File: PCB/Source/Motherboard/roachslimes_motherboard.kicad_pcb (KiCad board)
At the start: 2 copper layers, 34.5 x 49.9 mm, 13 parts, among them J1 Conn_01x04_Pin, J2 Conn_01x02_Pin, J3 Conn_01x03_Pin, SW1 SK12D07VG4, U1 WeMos_D1_mini, U2 TP4056_Board, U3 BMI160_Board, U4 GY-271

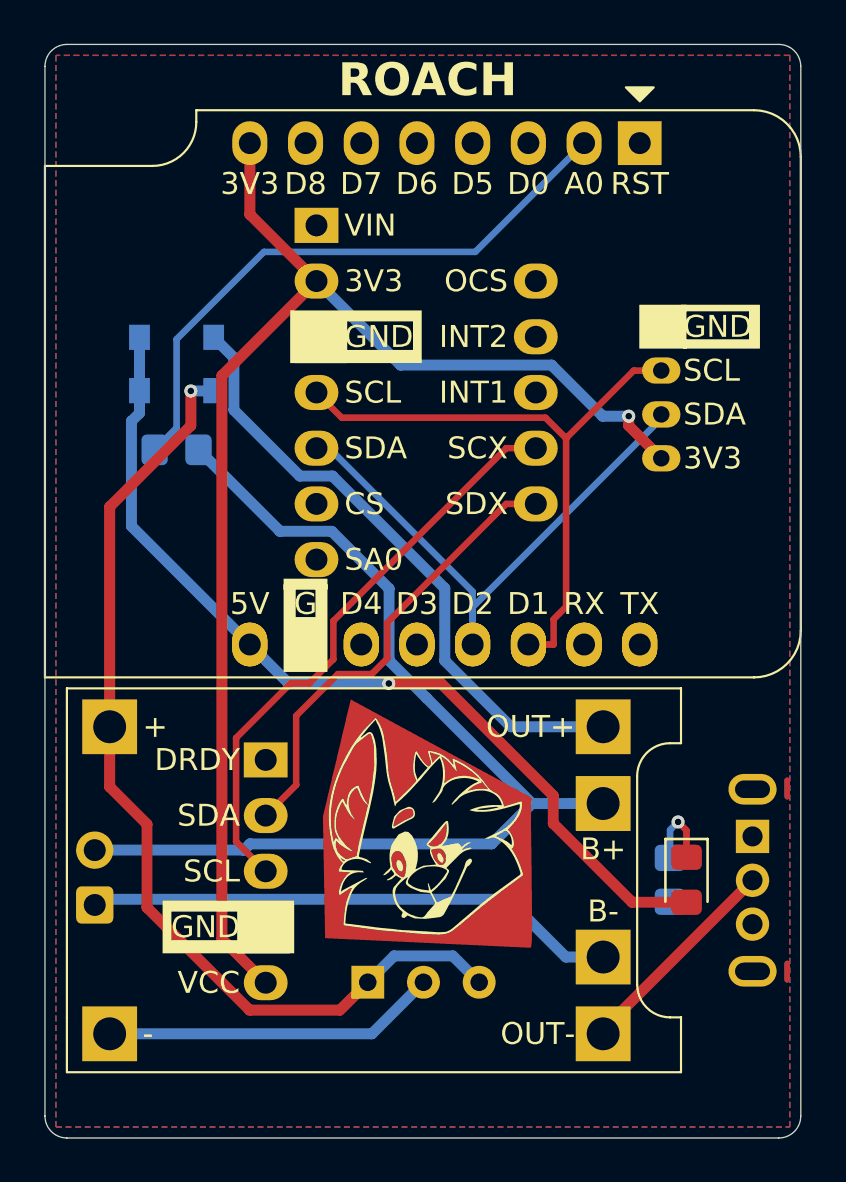
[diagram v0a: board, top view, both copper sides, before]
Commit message: fix minor spelling issues
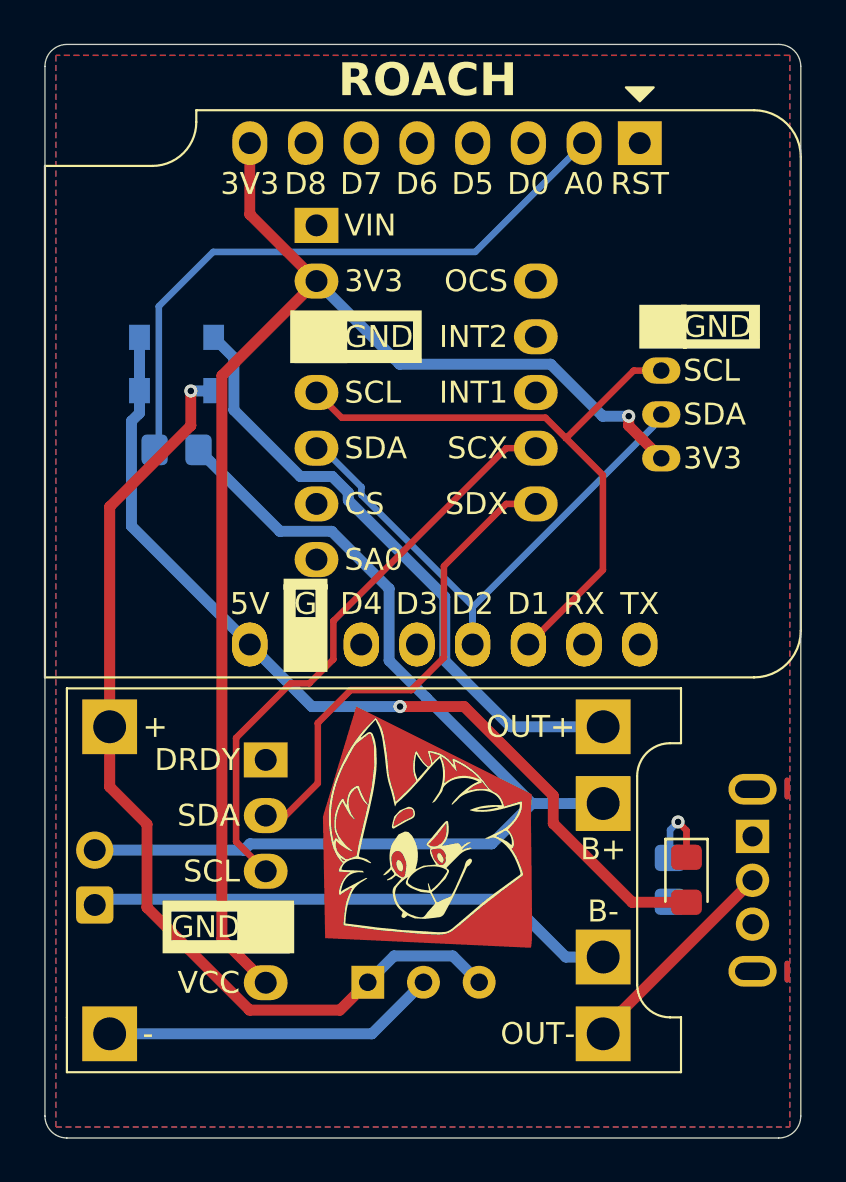
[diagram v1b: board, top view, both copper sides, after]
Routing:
- net /Sense: track 27.7 -> 29.1 mm
- net /SDX: track 21.0 -> 22.3 mm
- net /SCL: track 28.7 -> 29.4 mm
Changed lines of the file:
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@@
 	(gr_poly
 		(pts
-			(xy 89.695974 114.146309) (xy 89.677221 114.338624) (xy 89.665839 114.564175) (xy 89.660699 115.338384)
+			(xy 89.695974 113.989036) (xy 89.677221 114.338624) (xy 89.665839 114.564175) (xy 89.660699 115.338384)
 			(xy 89.689491 117.643062) (xy 89.710533 119.934801) (xy 89.695703 120.692836) (xy 89.678024 120.907873)
 			(xy 89.652005 120.988058) (xy 80.273537 120.549022) (xy 80.173044 115.009345) (xy 80.438475 115.009345)
@@
 			(xy 80.634372 113.682331) (xy 80.584762 113.869319) (xy 80.542011 114.057148) (xy 80.50633 114.24583)
 			(xy 80.477926 114.435379) (xy 80.45701 114.625806) (xy 80.44379 114.817124) (xy 80.438475 115.009345)
-			(xy 80.173044 115.009345) (xy 81.440846 109.666309)
+			(xy 80.173044 115.009345) (xy 81.690104 109.989036)
 		)
 		(stroke
@@
 	)
 	(segment
-		(start 94.2687 118.9125)
-		(end 96.75 118.9125)
+		(start 83.690104 109.989036)
+		(end 86.612049 109.989036)
 		(width 0.5)
 		(layer "F.Cu")
@@
 	)
 	(segment
-		(start 90.6748 115.3186)
-		(end 94.2687 118.9125)
+		(start 86.612049 109.989036)
+		(end 90.6748 114.051787)
 		(width 0.5)
 		(layer "F.Cu")
@@
 	)
 	(segment
-		(start 83.17719 108.937821)
-		(end 85.560834 108.937821)
+		(start 90.6748 114.051787)
+		(end 90.6748 115.3186)
 		(width 0.5)
 		(layer "F.Cu")
@@
 	)
 	(segment
-		(start 90.6748 114.051787)
-		(end 90.6748 115.3186)
+		(start 90.6748 115.3186)
+		(end 94.2687 118.9125)
 		(width 0.5)
 		(layer "F.Cu")
@@
 	)
 	(segment
-		(start 85.560834 108.937821)
-		(end 90.6748 114.051787)
+		(start 94.2687 118.9125)
+		(end 96.75 118.9125)
 		(width 0.5)
 		(layer "F.Cu")
@@
 	)
 	(via
-		(at 83.17719 108.937821)
+		(at 83.690104 109.989036)
 		(size 0.6)
 		(drill 0.3)
@@
 	)
 	(segment
-		(start 78.617821 108.937821)
-		(end 76.84 107.16)
+		(start 83.690104 109.989036)
+		(end 79.669036 109.989036)
 		(width 0.5)
 		(layer "B.Cu")
@@
 	)
 	(segment
-		(start 83.17719 108.937821)
-		(end 78.617821 108.937821)
+		(start 79.669036 109.989036)
+		(end 76.84 107.16)
 		(width 0.5)
 		(layer "B.Cu")
@@
 	)
 	(segment
-		(start 92.927767 96.75)
-		(end 90.597767 94.42)
+		(start 90.557767 94.38)
+		(end 83.67 94.38)
 		(width 0.5)
 		(layer "B.Cu")
@@
 	)
 	(segment
-		(start 90.597767 94.42)
-		(end 83.71 94.42)
+		(start 92.927767 96.75)
+		(end 90.557767 94.38)
 		(width 0.5)
 		(layer "B.Cu")
@@
 	)
 	(segment
-		(start 83.71 94.42)
+		(start 83.67 94.38)
 		(end 79.88 90.59)
 		(width 0.5)
@@
 	)
 	(segment
-		(start 87 107.16)
-		(end 87 104.75)
+		(start 81.93 99.983705)
+		(end 81.93 100.339352)
 		(width 0.3)
 		(layer "B.Cu")
@@
 	)
 	(segment
-		(start 79.88 98.21)
-		(end 80.46 98.21)
+		(start 80.156295 98.21)
+		(end 81.93 99.983705)
 		(width 0.3)
 		(layer "B.Cu")
@@
 	)
 	(segment
-		(start 80.46 98.21)
-		(end 87 104.75)
+		(start 87 105.409352)
+		(end 87 107.16)
 		(width 0.3)
 		(layer "B.Cu")
@@
 	)
 	(segment
+		(start 79.88 98.21)
+		(end 80.156295 98.21)
+		(width 0.3)
+		(layer "B.Cu")
+		(net 21)
+	)
+	(segment
+		(start 81.93 100.339352)
+		(end 87 105.409352)
+		(width 0.3)
+		(layer "B.Cu")
+		(net 21)
+	)
+	(segment
 		(start 70.45 110.91)
 		(end 70.45 113.648932)
@@
 	)
 	(segment
-		(start 88.7406 110.91)
-		(end 85.73 107.8994)
+		(start 80.597767 99.5)
+		(end 79.1423 99.5)
 		(width 0.5)
 		(layer "B.Cu")
@@
 	)
 	(segment
-		(start 85.73 104.5983)
-		(end 80.6117 99.48)
+		(start 76.115 94.08)
+		(end 75.19 93.155)
 		(width 0.5)
 		(layer "B.Cu")
@@
 	)
 	(segment
-		(start 76.115 96.4727)
-		(end 76.115 94.08)
+		(start 85.73 107.8994)
+		(end 85.73 104.98788)
 		(width 0.5)
 		(layer "B.Cu")
@@
 	)
 	(segment
-		(start 85.73 107.8994)
-		(end 85.73 104.5983)
+		(start 85.73 104.98788)
+		(end 81.33 100.58788)
 		(width 0.5)
 		(layer "B.Cu")
@@
 	)
 	(segment
-		(start 79.1223 99.48)
-		(end 76.115 96.4727)
+		(start 88.7406 110.91)
+		(end 85.73 107.8994)
 		(width 0.5)
 		(layer "B.Cu")
@@
 	)
 	(segment
-		(start 76.115 94.08)
-		(end 75.19 93.155)
+		(start 76.115 96.4727)
+		(end 76.115 94.08)
 		(width 0.5)
 		(layer "B.Cu")
@@
 	)
 	(segment
-		(start 80.6117 99.48)
-		(end 79.1223 99.48)
+		(start 92.95 110.91)
+		(end 88.7406 110.91)
 		(width 0.5)
 		(layer "B.Cu")
@@
 	)
 	(segment
-		(start 92.95 110.91)
-		(end 88.7406 110.91)
+		(start 81.33 100.58788)
+		(end 81.33 100.232233)
+		(width 0.5)
+		(layer "B.Cu")
+		(net 23)
+	)
+	(segment
+		(start 81.33 100.232233)
+		(end 80.597767 99.5)
+		(width 0.5)
+		(layer "B.Cu")
+		(net 23)
+	)
+	(segment
+		(start 79.1423 99.5)
+		(end 76.115 96.4727)
 		(width 0.5)
 		(layer "B.Cu")
@@
 	)
 	(segment
-		(start 83.115 107.791346)
-		(end 82.396346 108.51)
+		(start 78.46914 114.96)
+		(end 79.940104 113.489036)
 		(width 0.3)
 		(layer "F.Cu")
@@
 	)
 	(segment
-		(start 89.88 100.75)
-		(end 88.5283 100.75)
+		(start 85.690104 107.756242)
+		(end 85.690104 103.588196)
 		(width 0.3)
 		(layer "F.Cu")
@@
 	)
 	(segment
-		(start 78.9548 110.4102)
-		(end 78.9548 113.5702)
+		(start 77.565 114.96)
+		(end 78.46914 114.96)
 		(width 0.3)
 		(layer "F.Cu")
@@
 	)
 	(segment
-		(start 82.396346 108.51)
-		(end 80.855 108.51)
+		(start 79.940104 110.739036)
+		(end 81.440104 109.239036)
 		(width 0.3)
 		(layer "F.Cu")
@@
 	)
 	(segment
-		(start 78.9548 113.5702)
-		(end 77.565 114.96)
+		(start 85.690104 103.588196)
+		(end 88.5283 100.75)
 		(width 0.3)
 		(layer "F.Cu")
@@
 	(segment
 		(start 88.5283 100.75)
-		(end 83.115 106.1633)
+		(end 89.88 100.75)
 		(width 0.3)
 		(layer "F.Cu")
@@
 	)
 	(segment
-		(start 83.115 106.1633)
-		(end 83.115 107.791346)
+		(start 84.20731 109.239036)
+		(end 85.690104 107.756242)
 		(width 0.3)
 		(layer "F.Cu")
@@
 	)
 	(segment
-		(start 80.855 108.51)
-		(end 78.9548 110.4102)
+		(start 81.440104 109.239036)
+		(end 84.20731 109.239036)
 		(width 0.3)
 		(layer "F.Cu")
@@
 	)
 	(segment
-		(start 90.6917 107.16)
-		(end 90.6917 106.0083)
+		(start 79.940104 113.489036)
+		(end 79.940104 110.739036)
 		(width 0.3)
 		(layer "F.Cu")
-		(net 27)
+		(net 26)
 	)
 	(segment
@@
 	)
 	(segment
-		(start 89.54 107.16)
-		(end 90.6917 107.16)
+		(start 94.3472 94.67)
+		(end 91.26 97.7572)
 		(width 0.3)
 		(layer "F.Cu")
@@
 	)
 	(segment
-		(start 94.3472 94.67)
+		(start 92.940104 99.437304)
 		(end 91.26 97.7572)
 		(width 0.3)
@@
 	)
 	(segment
-		(start 91.26 105.44)
-		(end 91.26 97.7572)
+		(start 90.3245 96.8217)
+		(end 81.0317 96.8217)
 		(width 0.3)
 		(layer "F.Cu")
@@
 	)
 	(segment
-		(start 90.3245 96.8217)
-		(end 81.0317 96.8217)
+		(start 81.0317 96.8217)
+		(end 79.88 95.67)
 		(width 0.3)
 		(layer "F.Cu")
@@
 	)
 	(segment
-		(start 90.6917 106.0083)
-		(end 91.26 105.44)
+		(start 91.26 97.7572)
+		(end 90.3245 96.8217)
 		(width 0.3)
 		(layer "F.Cu")
@@
 	)
 	(segment
-		(start 81.0317 96.8217)
-		(end 79.88 95.67)
+		(start 92.940104 103.759896)
+		(end 92.940104 99.437304)
 		(width 0.3)
 		(layer "F.Cu")
@@
 	)
 	(segment
-		(start 91.26 97.7572)
-		(end 90.3245 96.8217)
+		(start 89.54 107.16)
+		(end 92.940104 103.759896)
 		(width 0.3)
 		(layer "F.Cu")
@@
 	)
 	(segment
-		(start 92.08 84.3)
-		(end 87.1199 89.2601)
+		(start 72.690104 98.094896)
+		(end 72.5 98.285)
 		(width 0.3)
 		(layer "B.Cu")
@@
 	)
 	(segment
-		(start 77.4839 89.2601)
-		(end 73.5 93.244)
+		(start 72.690104 91.739036)
+		(end 72.690104 98.094896)
 		(width 0.3)
 		(layer "B.Cu")
@@
 	)
 	(segment
-		(start 73.5 93.244)
-		(end 73.5 97.285)
+		(start 87.1199 89.2601)
+		(end 75.16904 89.2601)
 		(width 0.3)
 		(layer "B.Cu")
@@
 	)
 	(segment
-		(start 87.1199 89.2601)
-		(end 77.4839 89.2601)
+		(start 75.16904 89.2601)
+		(end 72.690104 91.739036)
 		(width 0.3)
 		(layer "B.Cu")
@@
 	)
 	(segment
-		(start 73.5 97.285)
-		(end 72.5 98.285)
+		(start 92.08 84.3)
+		(end 87.1199 89.2601)
 		(width 0.3)
 		(layer "B.Cu")
@@
 		(polygon
 			(pts
-				(xy 81.440846 109.766309) (xy 86.640846 112.616309) (xy 89.501522 114.21435) (xy 89.695703 120.692836)
+				(xy 81.690104 109.989036) (xy 86.640846 112.616309) (xy 89.501522 114.21435) (xy 89.695703 120.692836)
 				(xy 80.501522 120.31435) (xy 80.173044 115.009345)
 			)
